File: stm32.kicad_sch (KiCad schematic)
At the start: 62 parts, among them J401 Conn_02x07_Odd_Even, J402 Conn_01x02, J403 Conn_01x02, J404 Conn_01x07, J405 Conn_01x03, J406 Conn_01x07, J407 Conn_01x03, J408 Conn_01x05, J409 Conn_01x05, J410 Conn_01x04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

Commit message: Prof approved commit
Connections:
- net FROM_USR_BTN: now reaches JP403.1 (A), U401.3 (PC13)
- net VBAT renamed UP_VBAT
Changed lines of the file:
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@@
     (effects (font (size 3 3) (thickness 0.6) bold) (justify left bottom))
+  )
+  (label "FROM_USR_BTN" (at 118.11 71.12 90)
+    (effects (font (size 1.27 1.27)) (justify left bottom))
   )
   (global_label "I2C1_SDL" (shape input) (at 78.74 106.68 180) (fields_autoplaced)
@@
     )
   )
-  (global_label "VBAT" (shape input) (at 363.22 67.31 0) (fields_autoplaced)
+  (global_label "UP_VBAT" (shape input) (at 363.22 67.31 0) (fields_autoplaced)
     (effects (font (size 1.27 1.27)) (justify left))
-    (property "Intersheet References" "${INTERSHEET_REFS}" (id 0) (at 370.0479 67.2306 0)
+    (property "Intersheet References" "${INTERSHEET_REFS}" (id 0) (at 373.616 67.2306 0)
       (effects (font (size 1.27 1.27)) (justify left) hide)
     )
@@
     )
   )
-  (global_label "VBAT" (shape input) (at 88.9 30.48 90) (fields_autoplaced)
+  (global_label "UP_VBAT" (shape input) (at 88.9 30.48 90) (fields_autoplaced)
     (effects (font (size 1.27 1.27)) (justify left))
-    (property "Références Inter-Feuilles" "${INTERSHEET_REFS}" (id 0) (at 88.8206 23.6521 90)
+    (property "Références Inter-Feuilles" "${INTERSHEET_REFS}" (id 0) (at 88.8206 20.084 90)
       (effects (font (size 1.27 1.27)) (justify left) hide)
     )

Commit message: I2C bus correction & simplifaction
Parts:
- removed JP404: SolderJumper_2_Bridged, Jumper:SolderJumper-2_P1.3mm_Bridged2Bar_Pad1.0x1.5mm, symbol Jumper:SolderJumper_2_Bridged
- removed JP405, JP406, JP407, JP408, JP409: SolderJumper_2_Bridged, Jumper:SolderJumper-2_P1.3mm_Bridged_Pad1.0x1.5mm, symbol Jumper:SolderJumper_2_Bridged
- removed JP410, JP411: SolderJumper_2_Open, Jumper:SolderJumper-2_P1.3mm_Open_TrianglePad1.0x1.5mm, symbol Jumper:SolderJumper_2_Open
- removed L401: 600R @100MHz, Inductor_SMD:L_0603_1608Metric_Pad1.05x0.95mm_HandSolder, symbol Device:L_Small
- removed R415, R417: 1k, Resistor_SMD:R_0603_1608Metric_Pad0.98x0.95mm_HandSolder, symbol Device:R_Small
- removed R416, R418: 2k, Resistor_SMD:R_0603_1608Metric_Pad0.98x0.95mm_HandSolder, symbol Device:R_Small
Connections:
- net UP_VBAT is gone; now on net +3V3: C407.1, U401.6 (VBAT)
- net VREF is gone; now on net +3V3: C408.1, U401.7 (VREF+)
- net I2C1_SDA: now also R407.2
- net I2C1_SDL: now also R408.2
- net I2C2_SDA: now also R405.2
- net I2C2_SDL: now also R406.2
- net PROX_1: now also J407.1 (Pin_1)
- net PROX_2: now also J411.1 (Pin_1)
- net STLINK_RX: now also D404.1 (K)
- net STLINK_TX: now also D405.1 (K)

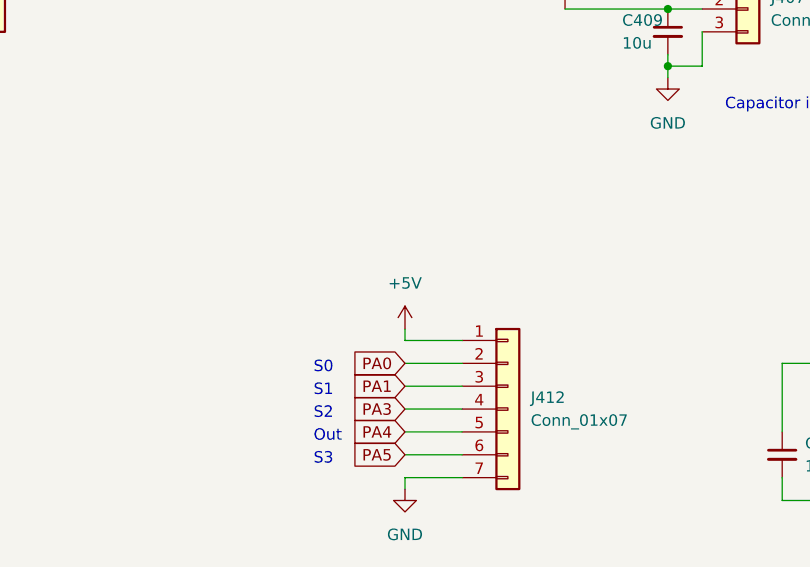
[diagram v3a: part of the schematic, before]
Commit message: Color sensor modif
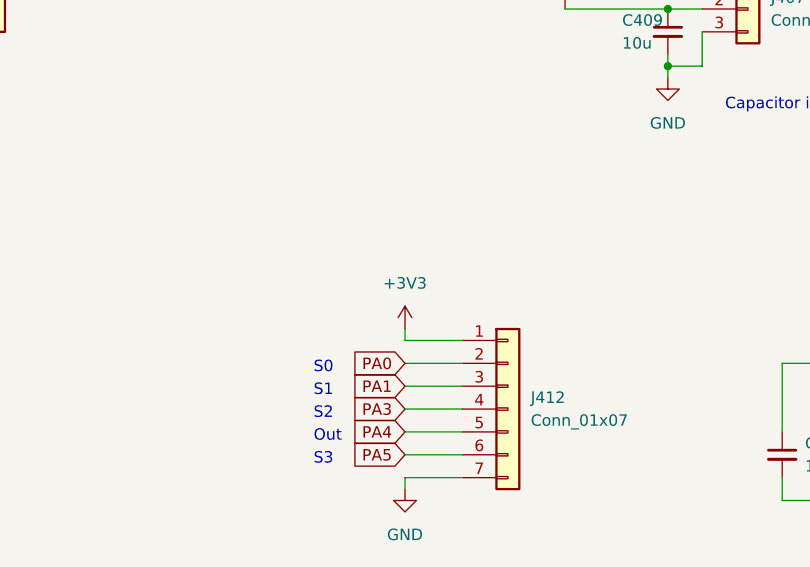
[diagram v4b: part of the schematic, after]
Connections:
- net +3V3: now also J412.1 (Pin_1)
- net +5V: no longer J412.1 (Pin_1)
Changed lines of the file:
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@@
-    (pin "1")
-  )
-  (symbol (lib_id "power:+5V") (at 302.26 223.52 0) (unit 1)
-    (in_bom yes) (on_board yes) (fields_autoplaced)
-    (property "Reference" "#PWR0426" (id 0) (at 302.26 227.33 0)
-      (effects (font (size 1.27 1.27)) hide)
-    )
-    (property "Value" "+5V" (id 1) (at 302.26 218.44 0))
-    (property "Footprint" "" (id 2) (at 302.26 223.52 0)
-      (effects (font (size 1.27 1.27)) hide)
-    )
-    (property "Datasheet" "" (id 3) (at 302.26 223.52 0)
-      (effects (font (size 1.27 1.27)) hide)
-    )
     (pin "1")
   )
@@
       (effects (font (size 1.27 1.27)) hide)
     )
+    (pin "1")
+  )
+  (symbol (lib_id "power:+3V3") (at 302.26 223.52 0) (unit 1)
+    (in_bom yes) (on_board yes) (fields_autoplaced)
+    (property "Reference" "#PWR?" (id 0) (at 302.26 227.33 0)
+      (effects (font (size 1.27 1.27)) hide)
+    )
+    (property "Value" "+3V3" (id 1) (at 302.26 218.44 0))
+    (property "Footprint" "" (id 2) (at 302.26 223.52 0)
+      (effects (font (size 1.27 1.27)) hide)
+    )
+    (property "Datasheet" "" (id 3) (at 302.26 223.52 0)
+      (effects (font (size 1.27 1.27)) hide)
+    )
